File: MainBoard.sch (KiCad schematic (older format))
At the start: 79 parts, among them J1 DB25, P1 BOOT, P10 CONN_01X03, P11 CONN_01X03, P12 CONN_01X03, P13 CONN_01X03, P14 CONN_01X02, P15 CONN_02X07, P16 CONN_02X05, P17 CONN_01X04, P18 CONN_01X03, P2 CONN_01X04, P3 CONN_01X05, P4 HOLE, P5 HOLE, P6 HOLE, P7 HOLE, P8 CONN_01X02, P9 CONN_01X03, Q1 BSS138, Q2 BSS138, Q3 DMN65D8L, SW1 RESET, U1 mp2307, U10 SI4425DDY, U2 DYS_mini_ESC, U3 DYS_mini_ESC, U4 DYS_mini_ESC, U5 DYS_mini_ESC, U6 TLV1117LV33, U7 TENDA_P200, U8 pca9685, U9 STM32F103CBT6, Y1 8MHz

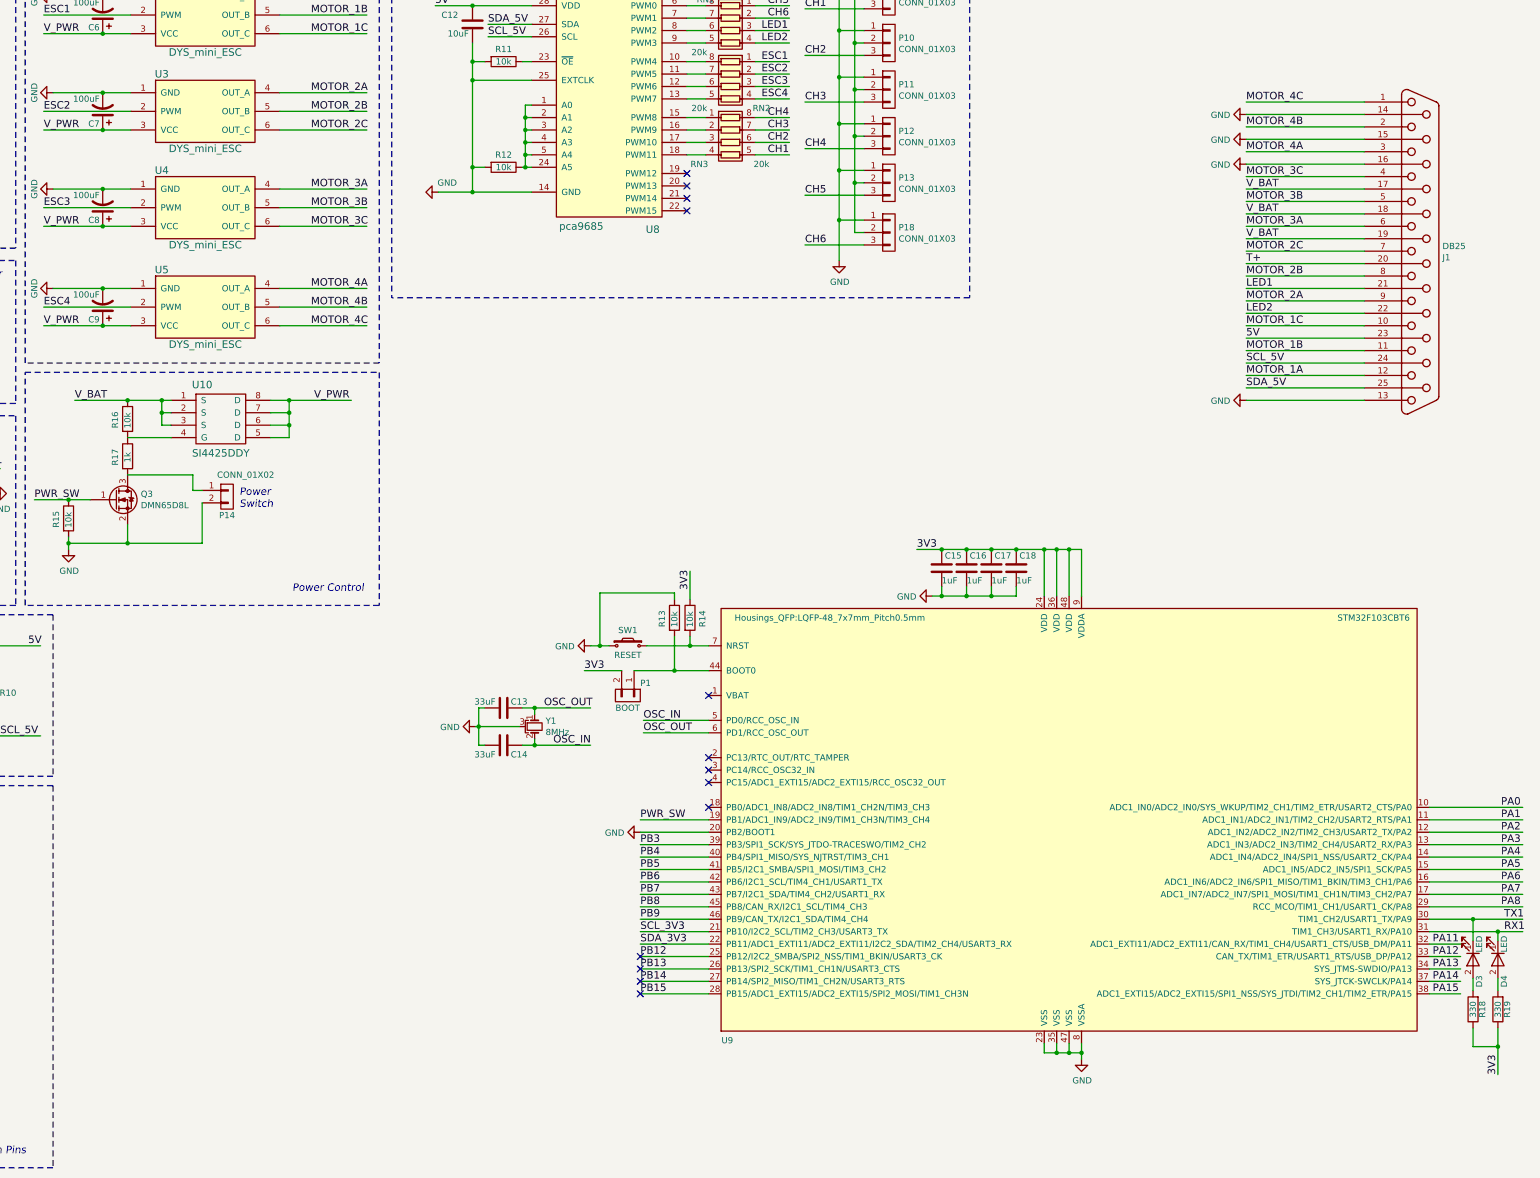
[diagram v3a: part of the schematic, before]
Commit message: change plc module position
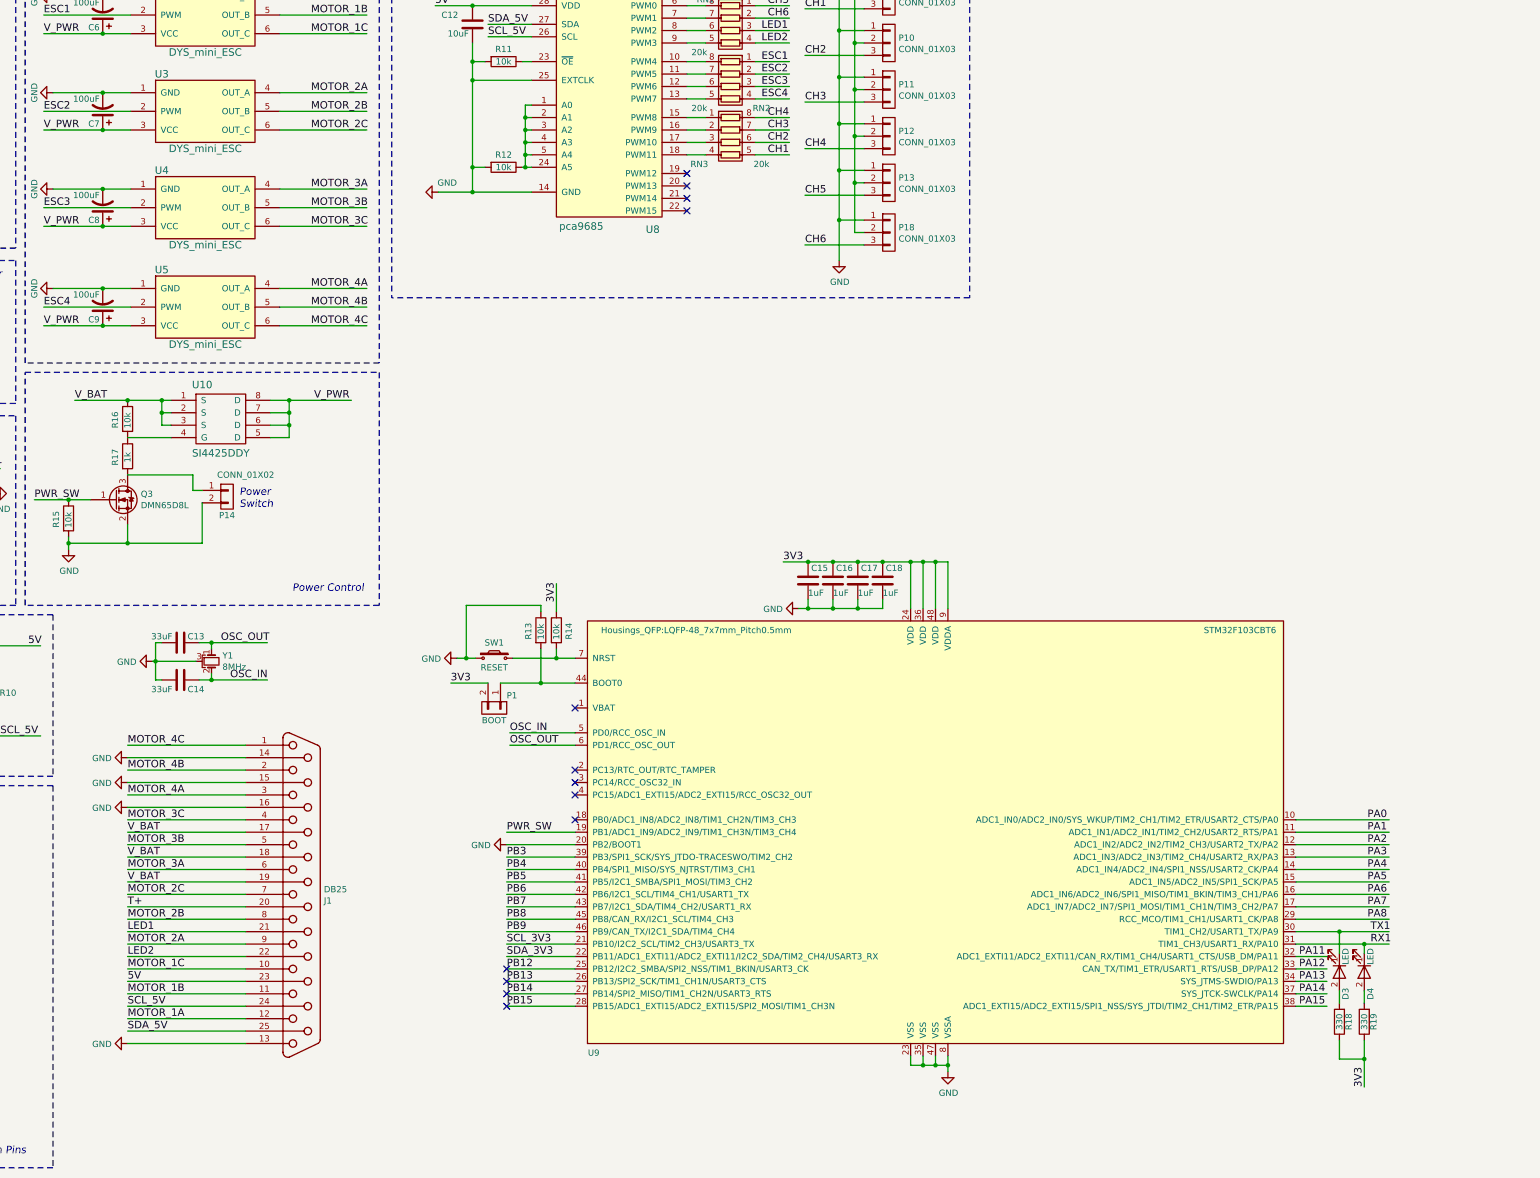
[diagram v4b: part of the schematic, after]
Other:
- moved on the sheet: C13, C14, C15, C16, C17, C18, D3, D4, J1, P1, R13, R14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

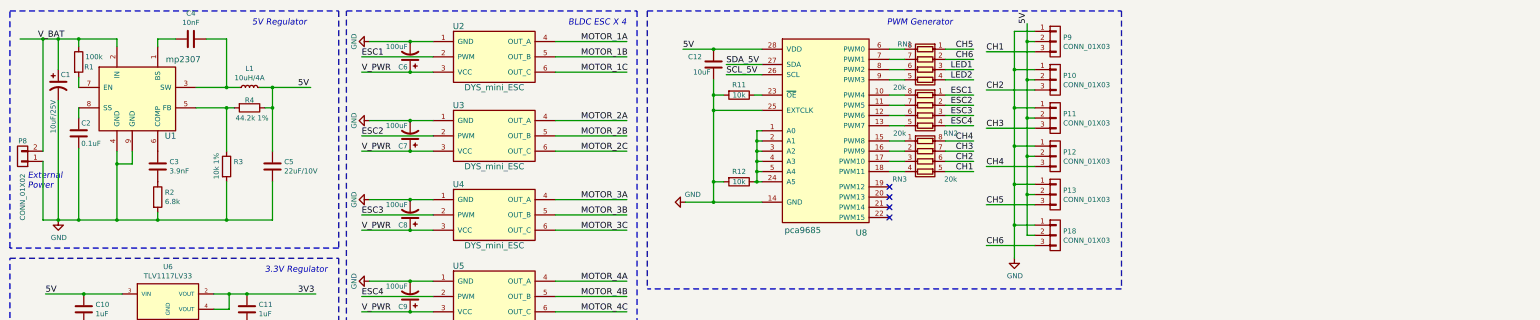
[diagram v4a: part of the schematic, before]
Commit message: change regulator position
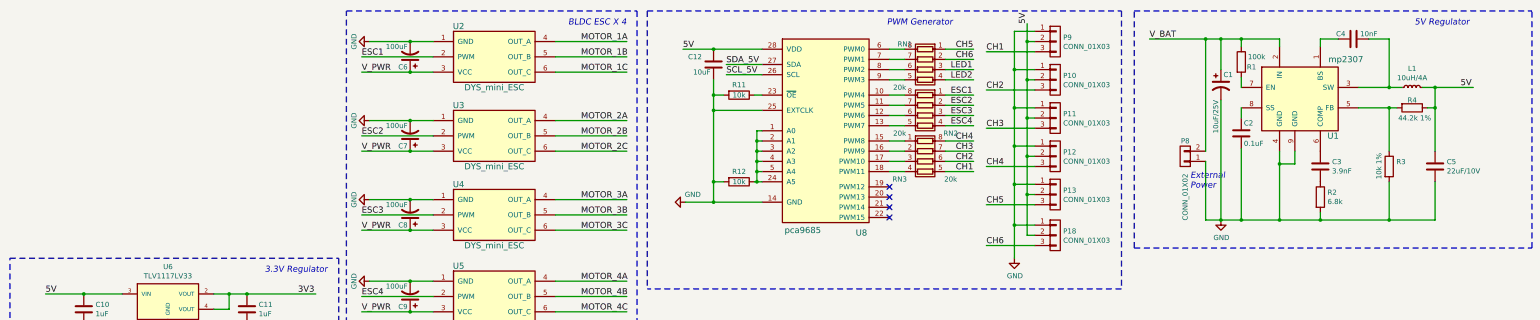
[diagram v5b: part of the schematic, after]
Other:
- moved on the sheet: C1, C2, C3, C4, C5, L1, P8, R1, R2, R3, R4, U1

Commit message: v.0.1
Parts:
- removed P3: CONN_01X05, Connectors_JST:JST_XH_B05B-XH-A_05x2.50mm_Straight, symbol CONN_01X05
- added C19: 220uF/10V, Capacitors_SMD:CP_Elec_6.3x5.8, symbol CP1
- added P3: CONN_02X04, Socket_Strips:Socket_Strip_Straight_2x04, symbol CONN_02X04
- P16: value CONN_02X05 -> CONN_02X04; footprint Socket_Strips:Socket_Strip_Straight_2x05 -> Socket_Strips:Socket_Strip_Straight_2x04; symbol CONN_02X05 -> CONN_02X04
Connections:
- net labels added: CH0, CH10, CH11, CH7, OSC_N, OSC_P, PB1
- net labels removed: OSC_IN, OSC_OUT, PB12
- wire segments 298 -> 300
- no-connect marks 19 -> 20
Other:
- moved on the sheet: C1, C12, C2, C3, C4, C5, L1, P10, P11, P12, P13, P18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

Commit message: routing...
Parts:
- removed P17: CONN_01X04, Connectors_JST:JST_XH_B04B-XH-A_04x2.50mm_Straight, symbol CONN_01X04
- removed R12: 10k, Capacitors_SMD:C_0603, symbol R
- added C21: 22uF/10V, Capacitors_SMD:C_0805, symbol C
- C6, C7, C8, C9: value 100uF -> 220uF/25V
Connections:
- net labels added: PB12
- net labels removed: PB1
- wire segments 300 -> 297
- no-connect marks 20 -> 21
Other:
- moved on the sheet: C13, C14, C15, C16, C17, C18, D3, D4, J1, P1, P15, P16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

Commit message: Add current & voltage sensor
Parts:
- added C20: 0.1uF, footprint:c_0603, symbol CP1
- added C22: 1uF, footprint:c_0603, symbol CP1
- added C23, C24: 0.1uF, footprint:c_0603, symbol C
- added R12: 0.003 %1, footprint:r_2512, symbol R
- added R20: 3.3k, footprint:r_0603, symbol R
- added R21: 30.1k %1, footprint:r_0603, symbol R
- added R22: 10k %1, footprint:r_0603, symbol R
- added U11: INA199A2, TO_SOT_Packages_SMD:SC-70-6, symbol INA199A2
- added U12: ADS1015, Housings_SSOP:MSOP-10_3x3mm_Pitch0.5mm, symbol ADS1015
- C1: footprint Capacitors_SMD:C_1206 -> footprint:c_1206
- C10, C11, C21, C5: footprint Capacitors_SMD:C_0805 -> footprint:c_0805
- C12, C15, C16, C17, C18, C2, C3, C4: footprint Capacitors_SMD:C_0603 -> footprint:c_0603
- C13, C14: value 33uF -> 33pF; footprint Capacitors_SMD:C_0603 -> footprint:c_0603
- R1, R10, R11, R13, R14, R15, R16, R17, R18, R19, R2, R3, R4, R5, R6, R7, R8, R9: footprint Capacitors_SMD:C_0603 -> footprint:r_0603
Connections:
- net labels added: ADC_I, ADC_V, V_IN
- wire segments 297 -> 330
- no-connect marks 21 -> 23
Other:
- note added: "16.7A full scale\nrange into 5V"
- note added: "20V full scale\ninto 5V"
- note added: "ADDR = 0x40"
- note added: "ADDR = 0x48"
- note added: "Current & Voltage sensing"
- note added: "LPF"
- moved on the sheet: C1, C12, C13, C14, C15, C16, C17, C18, C2, C21, C3, C4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
